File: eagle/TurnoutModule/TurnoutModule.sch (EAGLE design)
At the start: 15 parts, among them IC1 L293D, IC2 MCP23008/P

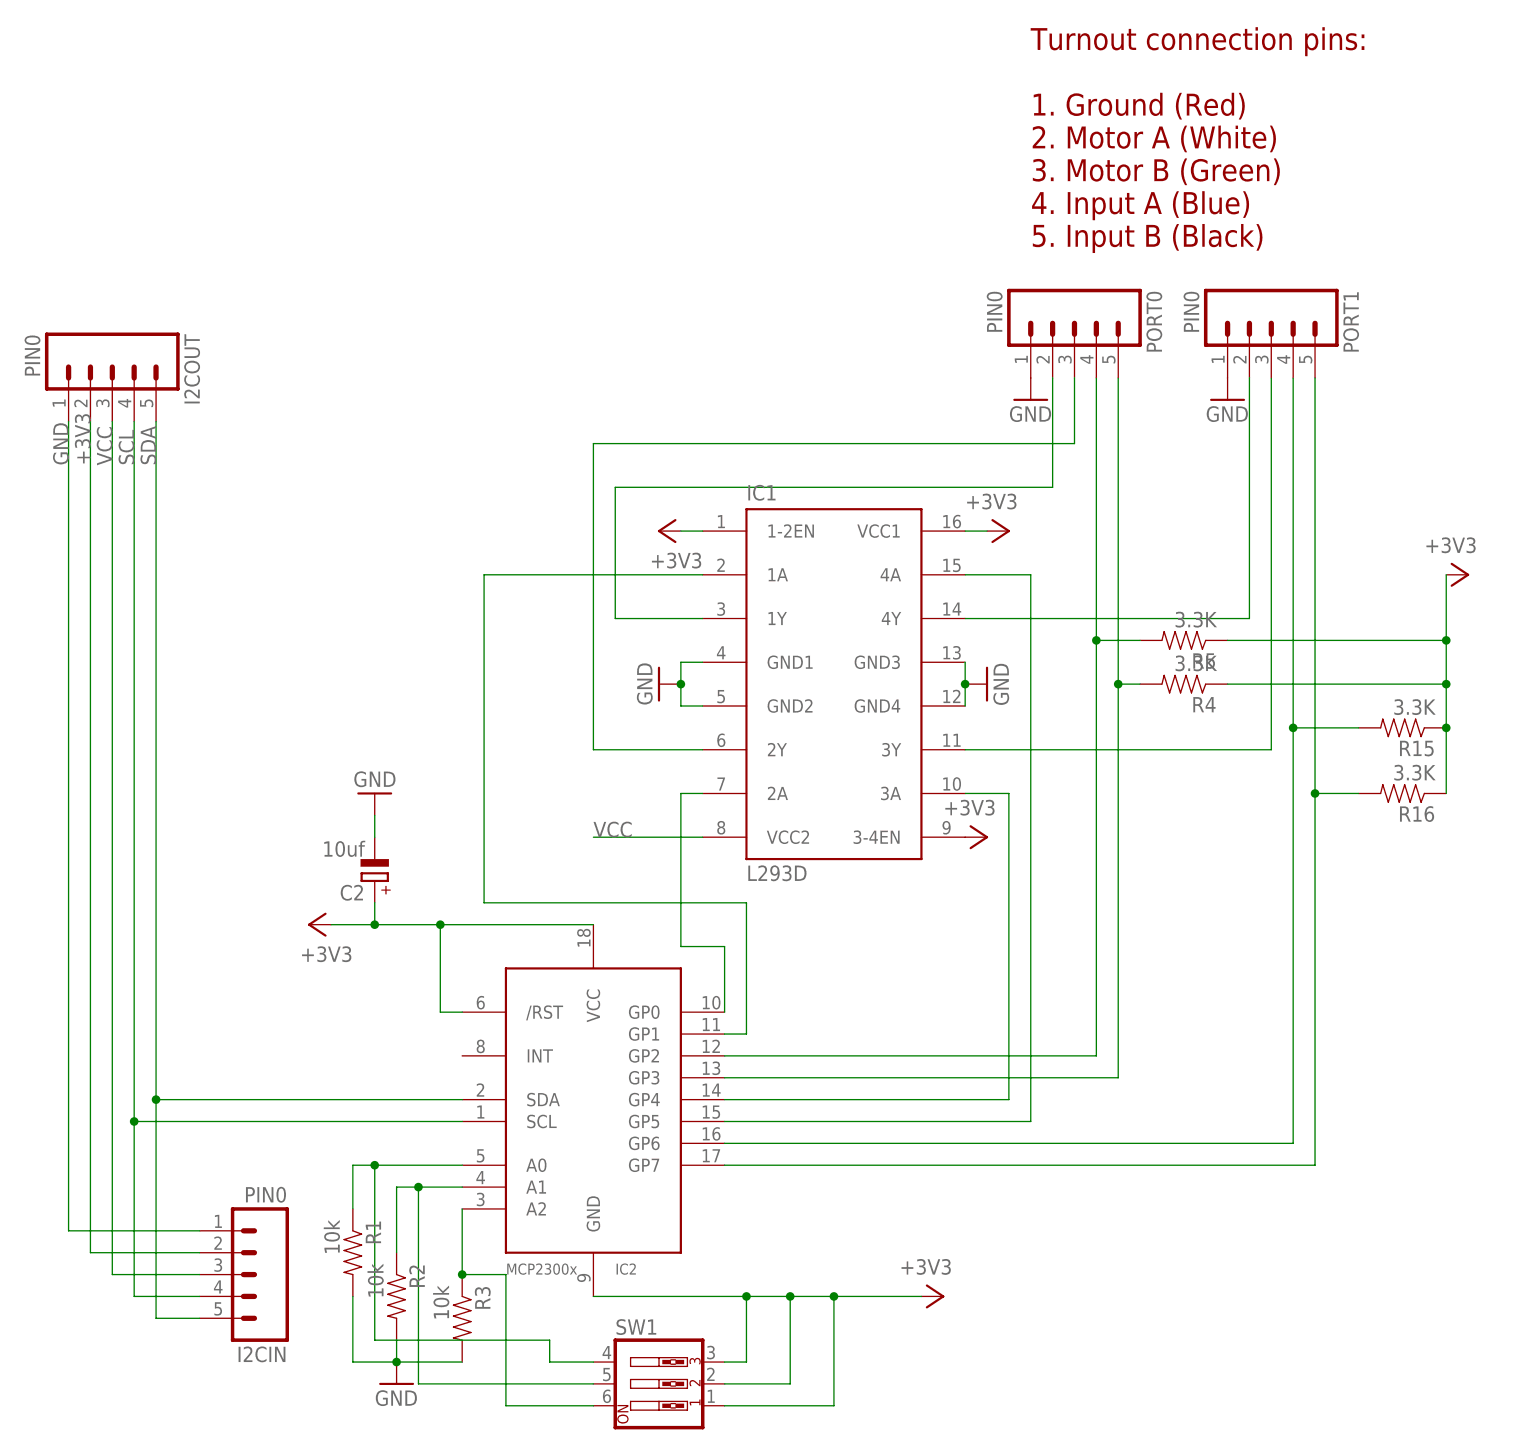
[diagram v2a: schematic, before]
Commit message: 1.  More adjustments to block detector 2.  Expander8 and Expander16 classes now impose a retry count.  More than three failed read/write attempts causes the module to be disabled. 3.  Signals now allow for both AND and OR conditions 4.  Fix TurnoutModule schematic and board layout for missing ground on expander chip 5.  NetworkManager now also detects WL_CONNECTION_LOST condition 6.  Database SignalCondition table updated with new conditionType field. 7.  Version change to 3.0.21
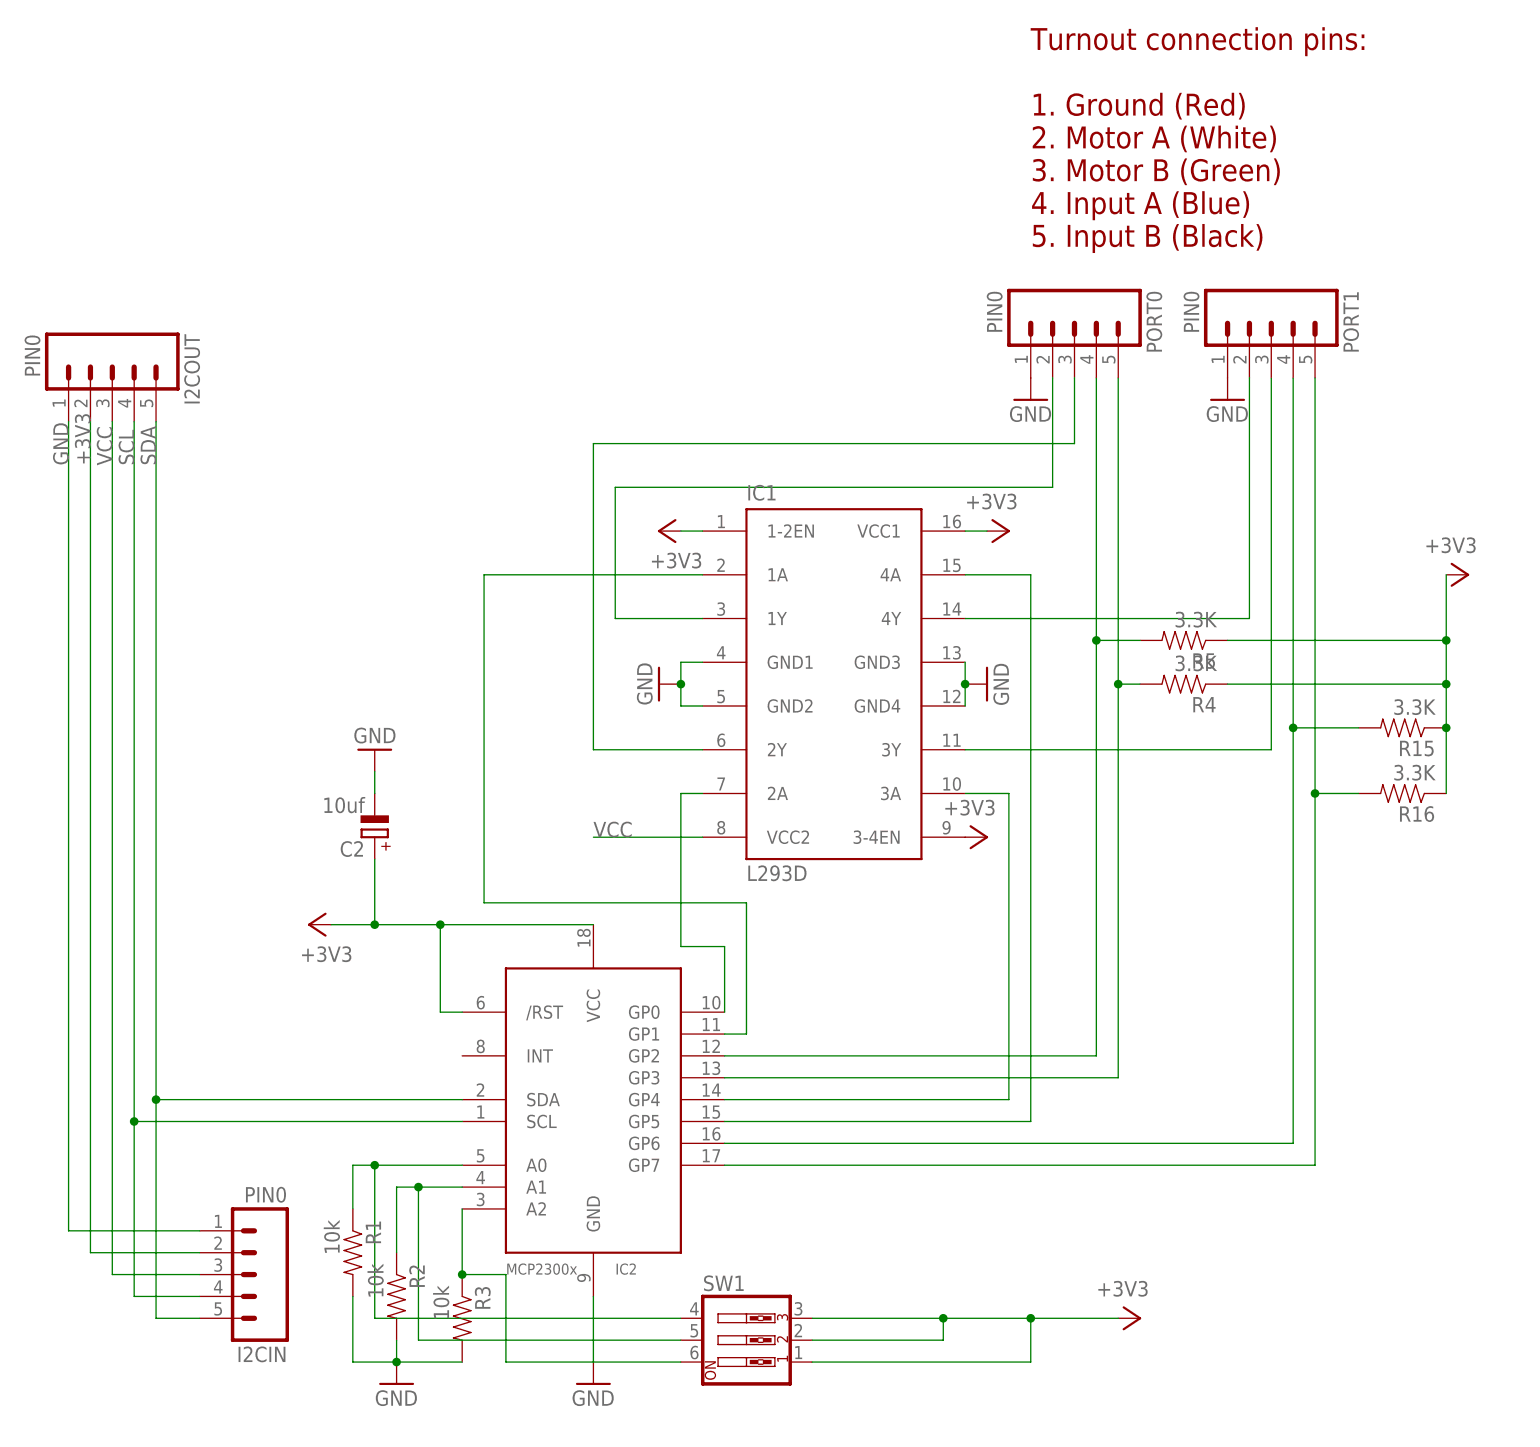
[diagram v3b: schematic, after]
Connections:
- net +3V3: no longer IC2.GND
- net GND: now also IC2.GND
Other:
- moved on the sheet: C2, SW1
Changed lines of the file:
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@@
 <part name="GND3" library="SparkFun-Aesthetics" deviceset="GND" device=""/>
 <part name="C2" library="rcl" deviceset="CPOL-EU" device="E2.5-6" value="10uf"/>
+<part name="GND4" library="SparkFun-Aesthetics" deviceset="GND" device=""/>
 </parts>
 <sheets>
@@
 <instance part="I2COUT" gate="G$1" x="-2.54" y="142.24" rot="R270"/>
 <instance part="I2CIN" gate="G$1" x="15.24" y="35.56" rot="R180"/>
-<instance part="GND1" gate="1" x="27.94" y="91.44" rot="R180"/>
+<instance part="GND1" gate="1" x="27.94" y="96.52" rot="R180"/>
 <instance part="R1" gate="G$1" x="25.4" y="38.1" rot="R270"/>
 <instance part="R2" gate="G$1" x="30.48" y="33.02" rot="R270"/>
 <instance part="R3" gate="G$1" x="38.1" y="30.48" rot="R270"/>
-<instance part="SW1" gate="A" x="60.96" y="22.86"/>
-<instance part="+3V1" gate="G$1" x="93.98" y="33.02" rot="R270"/>
+<instance part="SW1" gate="A" x="71.12" y="27.94"/>
+<instance part="+3V1" gate="G$1" x="116.84" y="30.48" rot="R270"/>
 <instance part="GND3" gate="1" x="30.48" y="22.86"/>
-<instance part="C2" gate="G$1" x="27.94" y="81.28" rot="R180"/>
+<instance part="C2" gate="G$1" x="27.94" y="86.36" rot="R180"/>
+<instance part="GND4" gate="1" x="53.34" y="22.86"/>
 </instances>
 <busses>
@@
 <segment>
 <pinref part="GND1" gate="1" pin="GND"/>
-<wire x1="27.94" y1="88.9" x2="27.94" y2="86.36" width="0.1524" layer="91"/>
+<wire x1="27.94" y1="93.98" x2="27.94" y2="91.44" width="0.1524" layer="91"/>
 <pinref part="C2" gate="G$1" pin="-"/>
 </segment>
@@
 <wire x1="30.48" y1="27.94" x2="30.48" y2="25.4" width="0.1524" layer="91"/>
 <pinref part="GND3" gate="1" pin="GND"/>
+</segment>
+<segment>
+<pinref part="GND4" gate="1" pin="GND"/>
+<pinref part="IC2" gate="G$1" pin="GND"/>
+<wire x1="53.34" y1="25.4" x2="53.34" y2="33.02" width="0.1524" layer="91"/>
 </segment>
 </net>
@@
 <wire x1="35.56" y1="66.04" x2="35.56" y2="76.2" width="0.1524" layer="91"/>
 <junction x="35.56" y="76.2"/>
-<wire x1="27.94" y1="76.2" x2="27.94" y2="78.74" width="0.1524" layer="91"/>
+<wire x1="27.94" y1="76.2" x2="27.94" y2="83.82" width="0.1524" layer="91"/>
 <junction x="27.94" y="76.2"/>
 <pinref part="C2" gate="G$1" pin="+"/>
@@
 </segment>
 <segment>
-<pinref part="IC2" gate="G$1" pin="GND"/>
-<wire x1="91.44" y1="33.02" x2="81.28" y2="33.02" width="0.1524" layer="91"/>
+<wire x1="114.3" y1="30.48" x2="104.14" y2="30.48" width="0.1524" layer="91"/>
 <pinref part="SW1" gate="A" pin="3"/>
-<wire x1="81.28" y1="33.02" x2="76.2" y2="33.02" width="0.1524" layer="91"/>
-<wire x1="76.2" y1="33.02" x2="71.12" y2="33.02" width="0.1524" layer="91"/>
-<wire x1="71.12" y1="33.02" x2="53.34" y2="33.02" width="0.1524" layer="91"/>
-<wire x1="68.58" y1="25.4" x2="71.12" y2="25.4" width="0.1524" layer="91"/>
-<wire x1="71.12" y1="25.4" x2="71.12" y2="33.02" width="0.1524" layer="91"/>
-<junction x="71.12" y="33.02"/>
+<wire x1="104.14" y1="30.48" x2="93.98" y2="30.48" width="0.1524" layer="91"/>
+<wire x1="93.98" y1="30.48" x2="78.74" y2="30.48" width="0.1524" layer="91"/>
 <pinref part="SW1" gate="A" pin="2"/>
-<wire x1="68.58" y1="22.86" x2="76.2" y2="22.86" width="0.1524" layer="91"/>
-<wire x1="76.2" y1="22.86" x2="76.2" y2="33.02" width="0.1524" layer="91"/>
-<junction x="76.2" y="33.02"/>
+<wire x1="78.74" y1="27.94" x2="93.98" y2="27.94" width="0.1524" layer="91"/>
+<wire x1="93.98" y1="27.94" x2="93.98" y2="30.48" width="0.1524" layer="91"/>
+<junction x="93.98" y="30.48"/>
 <pinref part="SW1" gate="A" pin="1"/>
-<wire x1="68.58" y1="20.32" x2="81.28" y2="20.32" width="0.1524" layer="91"/>
-<wire x1="81.28" y1="20.32" x2="81.28" y2="33.02" width="0.1524" layer="91"/>
-<junction x="81.28" y="33.02"/>
+<wire x1="78.74" y1="25.4" x2="104.14" y2="25.4" width="0.1524" layer="91"/>
+<wire x1="104.14" y1="25.4" x2="104.14" y2="30.48" width="0.1524" layer="91"/>
+<junction x="104.14" y="30.48"/>
 <pinref part="+3V1" gate="G$1" pin="+3V3"/>
 </segment>
@@
 <junction x="27.94" y="48.26"/>
 <pinref part="SW1" gate="A" pin="4"/>
-<wire x1="27.94" y1="27.94" x2="27.94" y2="48.26" width="0.1524" layer="91"/>
-<wire x1="53.34" y1="25.4" x2="48.26" y2="25.4" width="0.1524" layer="91"/>
-<wire x1="48.26" y1="25.4" x2="48.26" y2="27.94" width="0.1524" layer="91"/>
-<wire x1="48.26" y1="27.94" x2="27.94" y2="27.94" width="0.1524" layer="91"/>
+<wire x1="27.94" y1="30.48" x2="27.94" y2="48.26" width="0.1524" layer="91"/>
+<wire x1="63.5" y1="30.48" x2="27.94" y2="30.48" width="0.1524" layer="91"/>
 </segment>
 </net>
@@
 <wire x1="30.48" y1="45.72" x2="30.48" y2="38.1" width="0.1524" layer="91"/>
 <pinref part="SW1" gate="A" pin="5"/>
-<wire x1="53.34" y1="22.86" x2="33.02" y2="22.86" width="0.1524" layer="91"/>
-<wire x1="33.02" y1="22.86" x2="33.02" y2="45.72" width="0.1524" layer="91"/>
+<wire x1="63.5" y1="27.94" x2="33.02" y2="27.94" width="0.1524" layer="91"/>
+<wire x1="33.02" y1="27.94" x2="33.02" y2="45.72" width="0.1524" layer="91"/>
 <junction x="33.02" y="45.72"/>
 </segment>
@@
 <pinref part="R3" gate="G$1" pin="1"/>
 <wire x1="38.1" y1="43.18" x2="38.1" y2="35.56" width="0.1524" layer="91"/>
-<wire x1="43.18" y1="20.32" x2="43.18" y2="35.56" width="0.1524" layer="91"/>
+<wire x1="43.18" y1="25.4" x2="43.18" y2="35.56" width="0.1524" layer="91"/>
 <wire x1="43.18" y1="35.56" x2="38.1" y2="35.56" width="0.1524" layer="91"/>
 <junction x="38.1" y="35.56"/>
 <pinref part="SW1" gate="A" pin="6"/>
-<wire x1="53.34" y1="20.32" x2="43.18" y2="20.32" width="0.1524" layer="91"/>
-</segment>
-</net>
+<wire x1="63.5" y1="25.4" x2="43.18" y2="25.4" width="0.1524" layer="91"/>
+</segment>
+</net>
